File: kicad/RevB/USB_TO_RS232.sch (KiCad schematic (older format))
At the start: 14 parts, among them J1 USB_A, U1 FT232RL

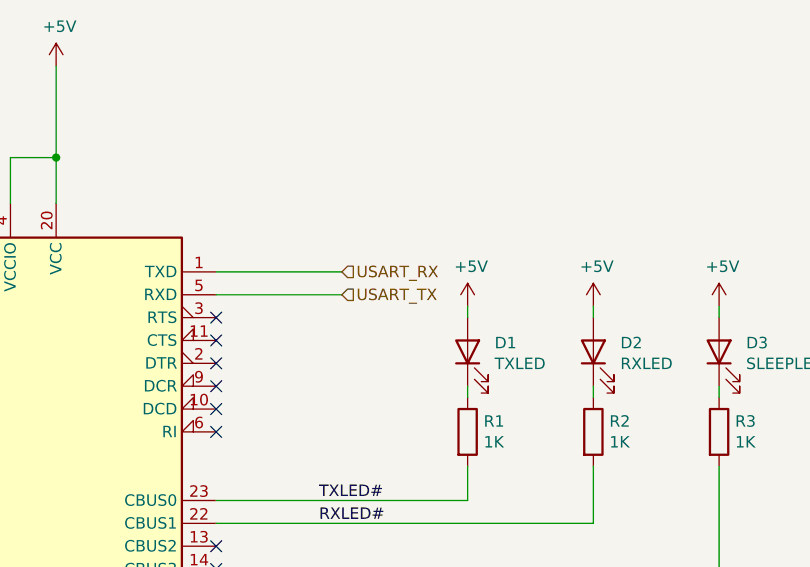
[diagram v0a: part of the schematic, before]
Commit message: updated hw
- corrected i2c pins
- changed reset btn to horizontal mount
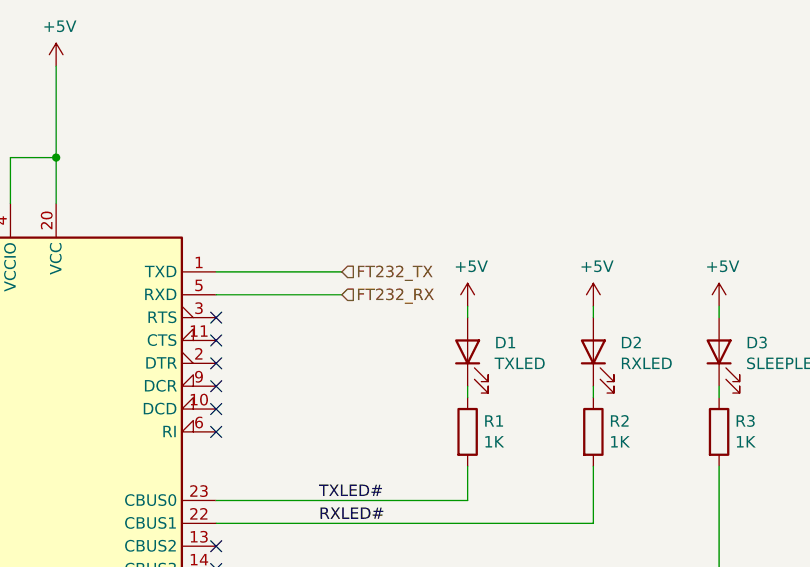
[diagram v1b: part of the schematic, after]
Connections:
- net USART_RX renamed FT232_TX
- net USART_TX renamed FT232_RX
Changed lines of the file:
@@
 $Descr A4 11693 8268
 encoding utf-8
-Sheet 2 4
+Sheet 4 4
 Title ""
 Date ""
@@
 	2250 4050 2600 4050
 Text HLabel 7250 2800 2    50   Input ~ 0
-USART_TX
+FT232_RX
 Text HLabel 7250 2700 2    50   Input ~ 0
-USART_RX
+FT232_TX
 $Comp
 L power:PWR_FLAG #FLG0102
